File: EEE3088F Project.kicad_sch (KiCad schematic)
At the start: 29 parts, among them J1 Conn_02x16_Odd_Even, J2 Battery IN JST, M1Control1 DRV8837, M2Control1 DRV8837, M3Control1 DRV8837, M4Control1 DRV8837, Q1 AO3400A, U1 TP4056-42-ESOP8, U2 TPS62163DSG

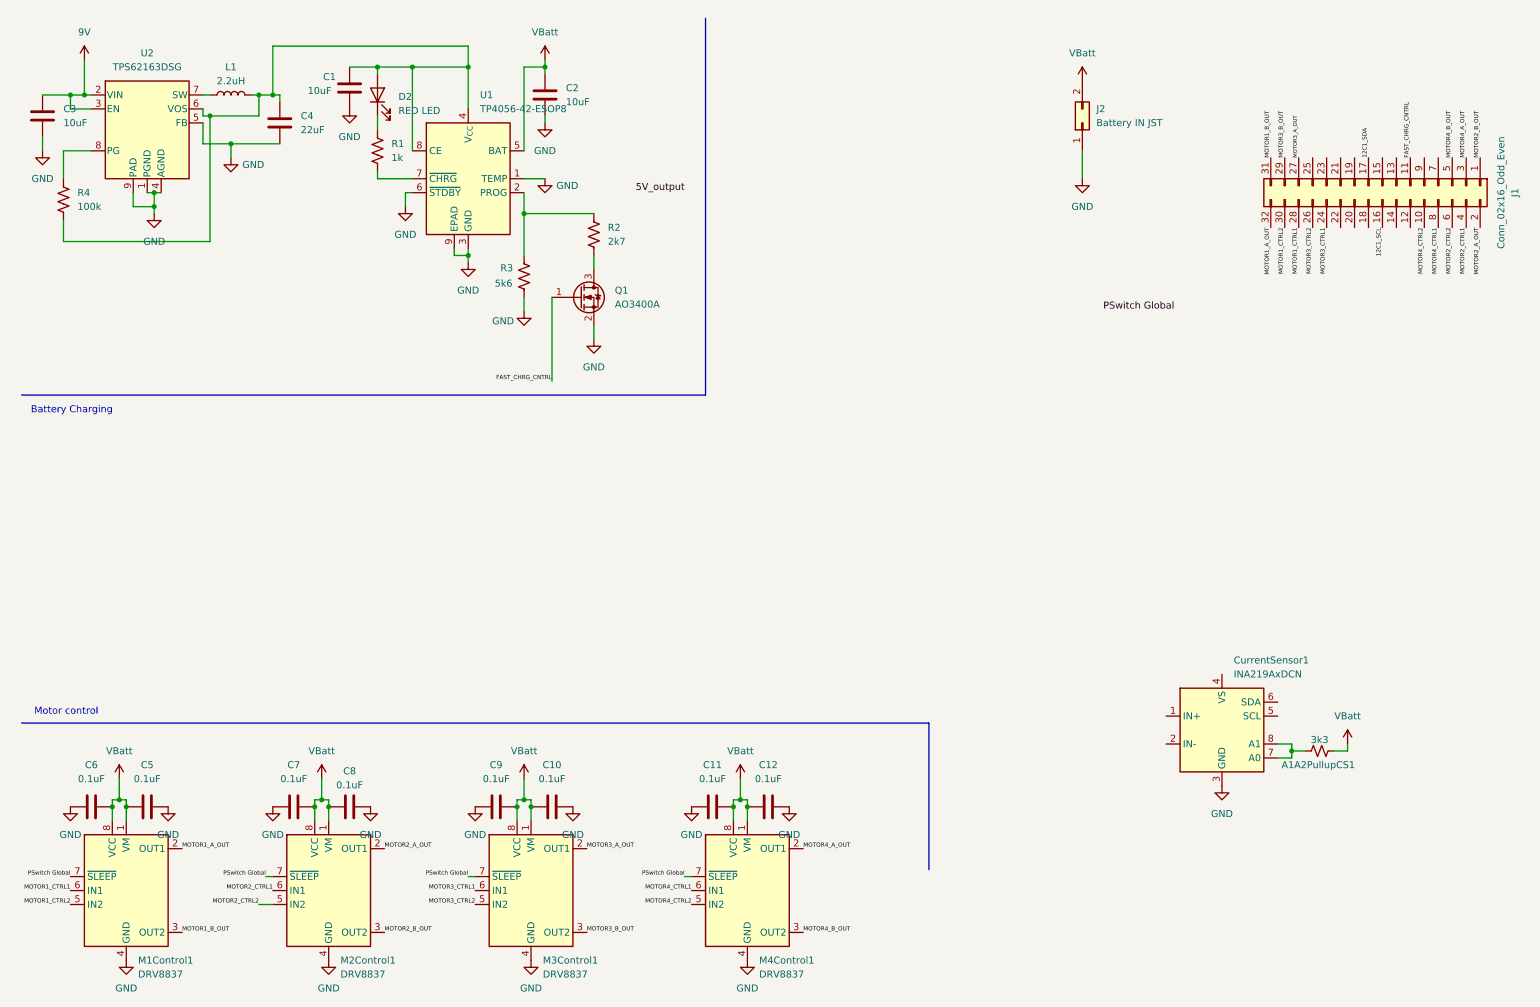
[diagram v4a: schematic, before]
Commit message: Finished current sensor circuit, finished battery connector circuit. Added footprints and BOM info for all.
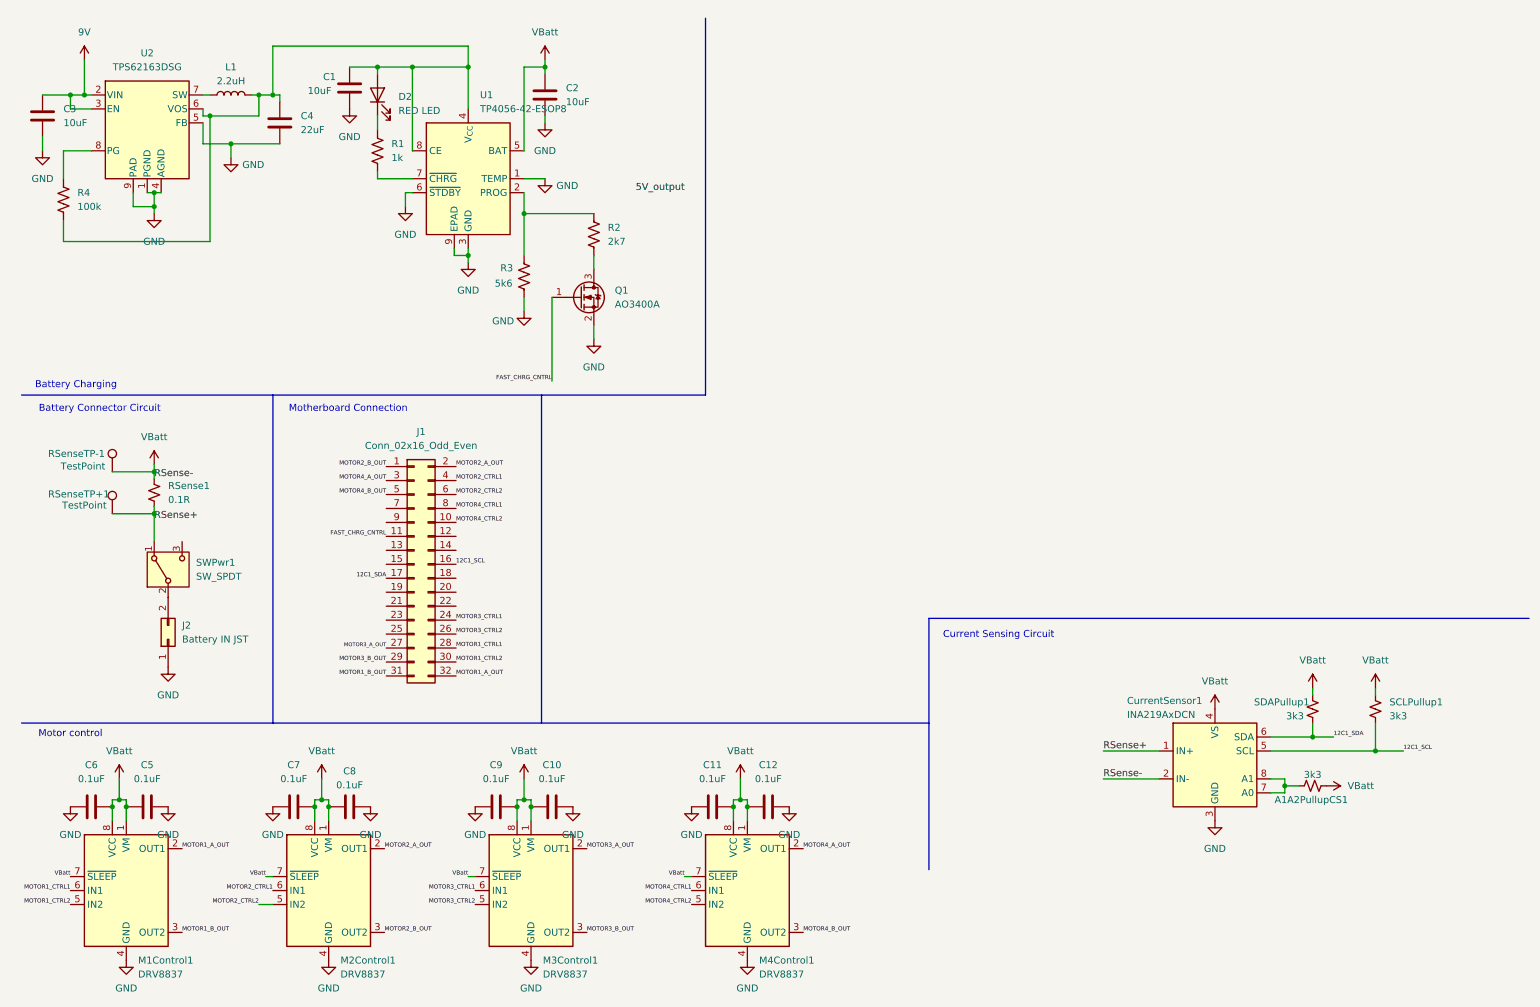
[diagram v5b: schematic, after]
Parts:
- added RSense1: 0.1R, Resistor_SMD:R_1206_3216Metric_Pad1.30x1.75mm_HandSolder, symbol Device:R_Small_US
- added RSenseTP+1, RSenseTP-1: TestPoint, TestPoint:TestPoint_Pad_2.0x2.0mm, symbol Connector:TestPoint
- added SCLPullup1, SDAPullup1: 3k3, Resistor_SMD:R_0603_1608Metric_Pad0.98x0.95mm_HandSolder, symbol Device:R_Small_US
- added SWPwr1: SW_SPDT, Custom Footprints:SW-TH_5P-P4.70_SS-12D11-G050, symbol Switch:SW_SPDT
- A1A2PullupCS1: footprint (none) -> Resistor_SMD:R_0603_1608Metric_Pad0.98x0.95mm_HandSolder
- J1: footprint (none) -> Connector_PinSocket_2.54mm:PinSocket_2x16_P2.54mm_Vertical
- J2: footprint (none) -> Connector_PinSocket_2.00mm:PinSocket_1x02_P2.00mm_Vertical
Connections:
- net PSwitch Global is gone; now on net VBatt: M1Control1.7 (~{SLEEP}), M2Control1.7 (~{SLEEP}), M3Control1.7 (~{SLEEP}), M4Control1.7 (~{SLEEP})
- net 12C1_SCL: now also CurrentSensor1.5 (SCL), SCLPullup1.2
- net 12C1_SDA: now also CurrentSensor1.6 (SDA), SDAPullup1.2
- net VBatt: now also CurrentSensor1.2 (IN-), CurrentSensor1.4 (VS), RSense1.1, RSenseTP-1.1, SCLPullup1.1, SDAPullup1.1; no longer J2.2 (Pin_2)
- net RSense+: now reaches CurrentSensor1.1 (IN+)
- net RSense+: now also RSense1.2, RSenseTP+1.1, SWPwr1.1 (A)
- new net: J2.2 (Pin_2), SWPwr1.2 (B)
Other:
- note added: "Battery Connector Circuit"
- note added: "Current Sensing Circuit"
- note added: "Motherboard Connection"
- moved on the sheet: A1A2PullupCS1, CurrentSensor1, J1, J2

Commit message: added 3V3 and 5V out circuitry as well as USBC
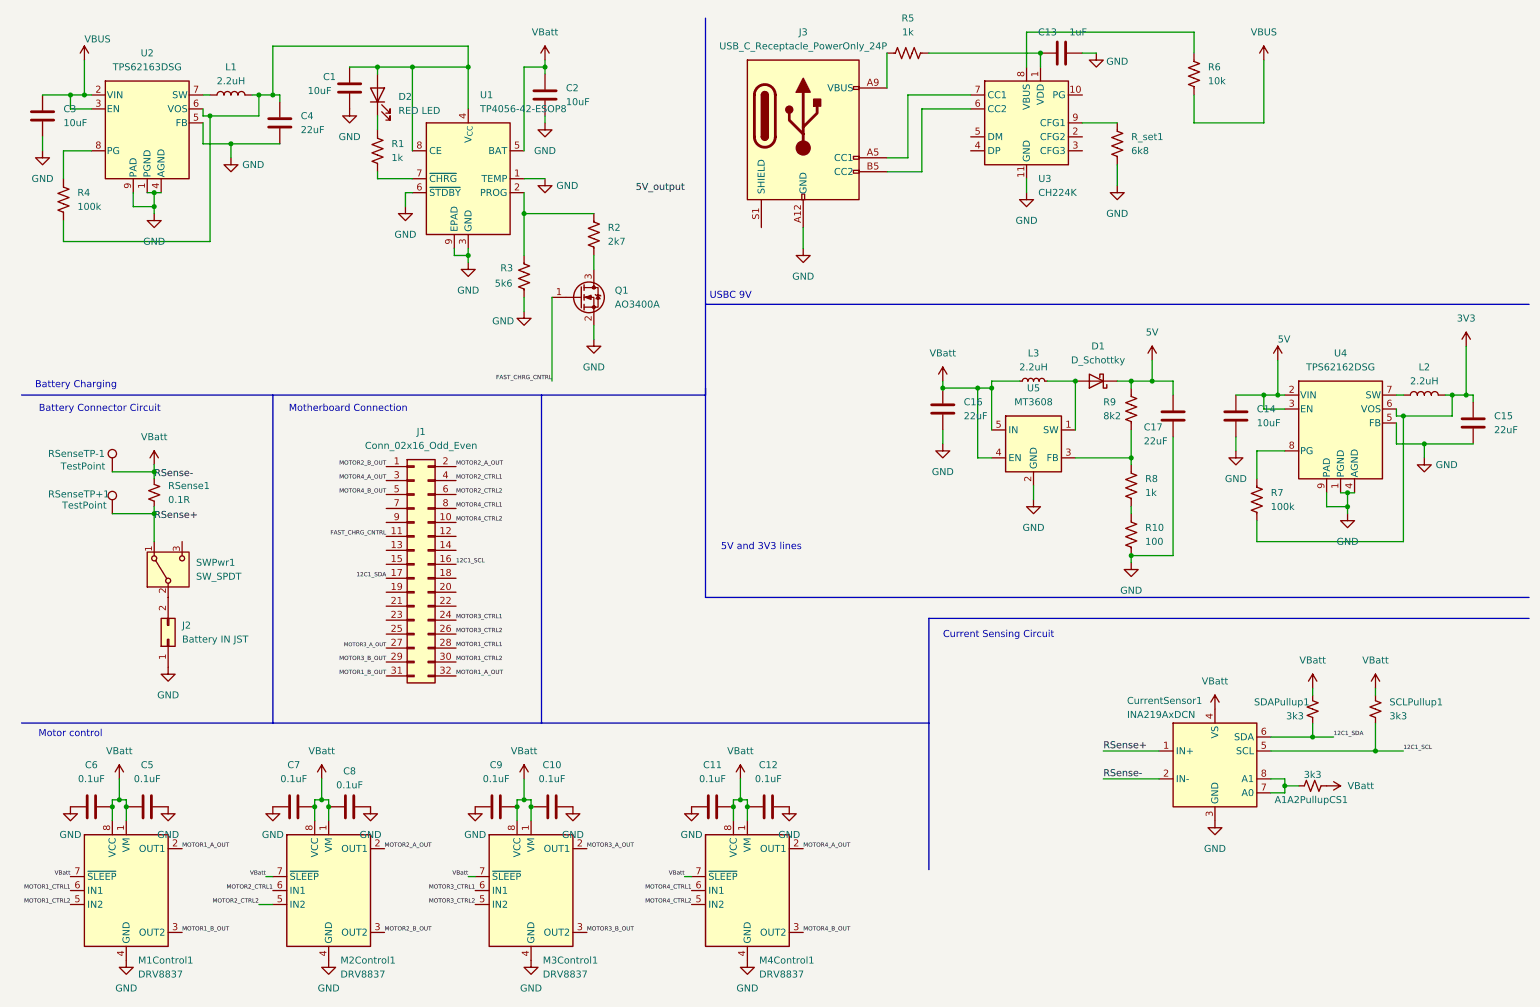
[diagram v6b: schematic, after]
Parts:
- added C13: 1uF, Capacitor_SMD:C_0603_1608Metric_Pad1.08x0.95mm_HandSolder, symbol Device:C
- added C14: 10uF, Capacitor_SMD:C_0805_2012Metric_Pad1.18x1.45mm_HandSolder, symbol Device:C
- added C15, C16, C17: 22uF, Capacitor_SMD:C_1206_3216Metric_Pad1.33x1.80mm_HandSolder, symbol Device:C
- added D1: D_Schottky, Diode_SMD:D_2512_6332Metric_Pad1.52x3.35mm_HandSolder, symbol Device:D_Schottky
- added J3: USB_C_Receptacle_PowerOnly_24P, Connector_USB:USB_C_Receptacle_Amphenol_124019772112A, symbol Connector:USB_C_Receptacle_PowerOnly_24P
- added L2: 2.2uH, Inductor_SMD:L_Taiyo-Yuden_MD-3030, symbol Device:L
- added L3: 2.2uH, Inductor_SMD:L_Taiyo-Yuden_MD-3030, symbol Device:L_Small
- added R10: 100, Resistor_SMD:R_0603_1608Metric_Pad0.98x0.95mm_HandSolder, symbol Device:R_US
- added R5, R8: 1k, Resistor_SMD:R_0603_1608Metric_Pad0.98x0.95mm_HandSolder, symbol Device:R_US
- added R6: 10k, Resistor_SMD:R_0603_1608Metric_Pad0.98x0.95mm_HandSolder, symbol Device:R_US
- added R7: 100k, Resistor_SMD:R_0603_1608Metric_Pad0.98x0.95mm_HandSolder, symbol Device:R_US
- added R9: 8k2, Resistor_SMD:R_0603_1608Metric_Pad0.98x0.95mm_HandSolder, symbol Device:R_US
- added R_set1: 6k8, Resistor_SMD:R_0603_1608Metric_Pad0.98x0.95mm_HandSolder, symbol Device:R_US
- added U3: CH224K, Package_SO:SSOP-10-1EP_3.9x4.9mm_P1mm_EP2.1x3.3mm, symbol Interface_USB:CH224K
- added U4: TPS62162DSG, Package_SON:WSON-8-1EP_2x2mm_P0.5mm_EP0.9x1.6mm_ThermalVias, symbol Regulator_Switching:TPS62162DSG
- added U5: MT3608, Package_TO_SOT_SMD:SOT-23-6, symbol Regulator_Switching:MT3608
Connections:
- net GND: now also C13.2, C14.2, C15.2, C16.2, C17.2, J3.A1 (GND), J3.A12 (GND), J3.B1 (GND), J3.B12 (GND), R10.2, R_set1.2, U3.11 (GND), U4.1 (PGND), U4.4 (AGND), U4.5 (FB), U4.9 (PAD), U5.2 (GND)
- net VBatt: now also C16.1, L3.1, U5.4 (EN), U5.5 (IN)
- net 9V renamed VBUS
- net VBUS: now also R6.2
- new net: D1.2 (A), L3.2, U5.1 (SW)
- new net: R6.1, U3.8 (VBUS)
- new net: C13.1, R5.2, U3.1 (VDD)
- new net: J3.B5 (CC2), U3.6 (CC2)
- new net: J3.A5 (CC1), U3.7 (CC1)
- new net: R_set1.1, U3.9 (CFG1)
- new net: L2.1, U4.7 (SW)
- new net: R7.1, U4.8 (PG)
- new net: R8.1, R9.2, U5.3 (FB)
- new net: J3.A4 (VBUS), J3.A9 (VBUS), J3.B4 (VBUS), J3.B9 (VBUS), R5.1
- new net: R10.1, R8.2
- new net 3V3: C15.1, L2.2, R7.2, U4.6 (VOS)
- new net 5V: C14.1, C17.1, D1.1 (K), R9.1, U4.2 (VIN), U4.3 (EN)
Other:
- note added: "5V and 3V3 lines"
- note added: "USBC 9V"

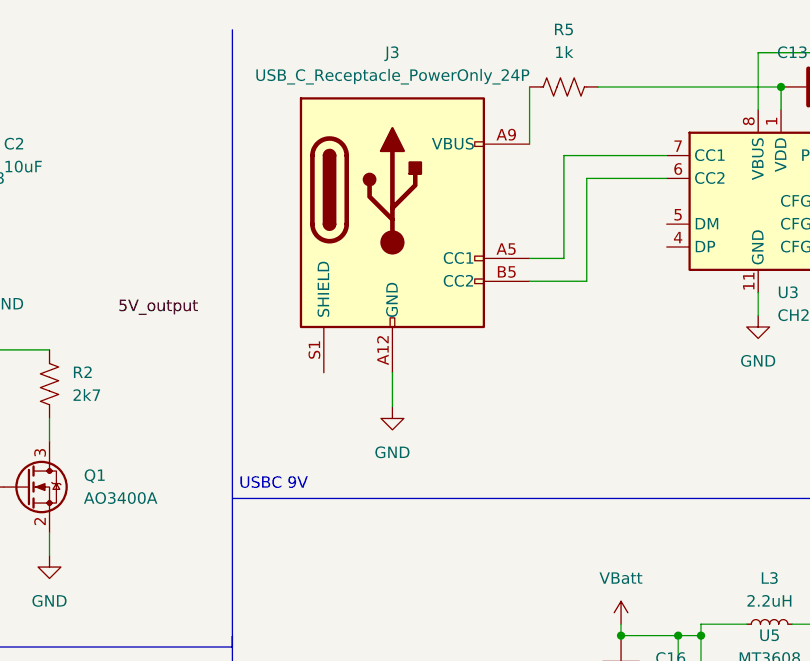
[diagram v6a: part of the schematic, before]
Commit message: corrected footprints for usbc and schottky diode
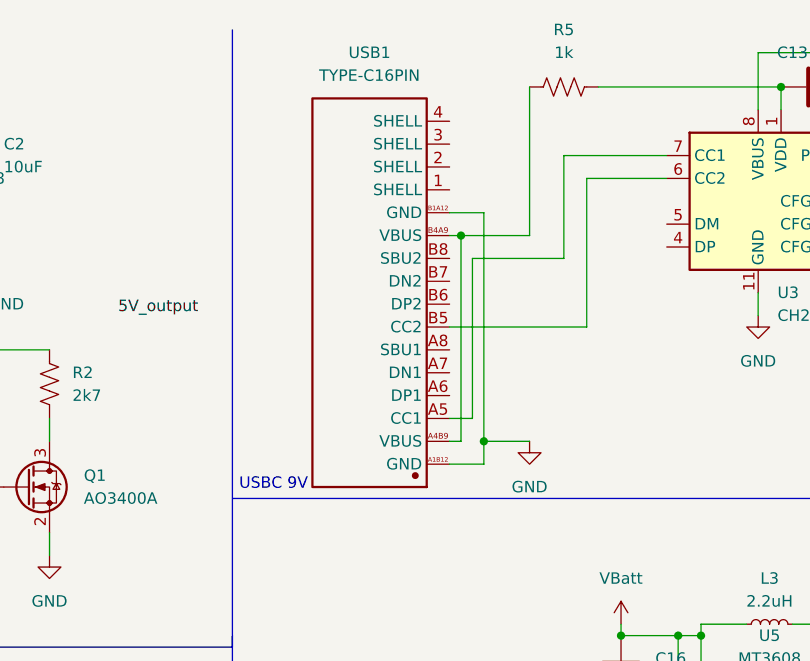
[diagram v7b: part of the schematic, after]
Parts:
- removed J3: USB_C_Receptacle_PowerOnly_24P, Connector_USB:USB_C_Receptacle_Amphenol_124019772112A, symbol Connector:USB_C_Receptacle_PowerOnly_24P
- added USB1: TYPE-C16PIN, TYPE-C16PIN__:USB-C-SMD_TYPE-C16PIN, symbol TYPE-C16PIN__:TYPE-C16PIN
- D1: footprint Diode_SMD:D_2512_6332Metric_Pad1.52x3.35mm_HandSolder -> SMA_L4.3-W2.6-LS5.2-RD:SMA_L4.3-W2.6-LS5.2-RD
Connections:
- net GND: now also USB1.A1B12 (GND), USB1.B1A12 (GND)
- net at U3.6 (CC2): now also USB1.B5 (CC2)
- net at U3.7 (CC1): now also USB1.A5 (CC1)
- net at R5.1: now also USB1.A4B9 (VBUS), USB1.B4A9 (VBUS)

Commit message: added custom symbol and placed usbc and schottky custom footprints into custom footprints.pretty
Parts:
- removed USB1: TYPE-C16PIN, TYPE-C16PIN__:USB-C-SMD_TYPE-C16PIN, symbol TYPE-C16PIN__:TYPE-C16PIN
- added USB1: TYPE-C16PIN, Custom Footprints:USB-C-SMD_TYPE-C16PIN, symbol Custom Symbols:TYPE-C16PIN
- D1: footprint SMA_L4.3-W2.6-LS5.2-RD:SMA_L4.3-W2.6-LS5.2-RD -> Custom Footprints:SMA_L4.3-W2.6-LS5.2-RD
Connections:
- net GND: now also USB1.A1B12 (GND), USB1.B1A12 (GND)
- net at U3.6 (CC2): now also USB1.B5 (CC2)
- net at U3.7 (CC1): now also USB1.A5 (CC1)
- net at R5.1: now also USB1.A4B9 (VBUS), USB1.B4A9 (VBUS)
